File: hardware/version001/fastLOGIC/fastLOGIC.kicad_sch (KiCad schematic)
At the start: 82 parts, among them J1 AVR-ISP-6, J10 0-5V_ANALOG_IN_A, J11 PRES_SENS_BOTTOM, J12 PRES_SENS_TOP, J13 0-5V_ANALOG_IN_B, J14 RELAY_OUT_B, J15 RELAY_OUT_A, J2 USB_B_Micro, J3 DS18B20, J4 12-24V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

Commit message: hardware chnages minor
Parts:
- removed J2: USB_B_Micro, Connector_USB:USB_Micro-B_Amphenol_10118194_Horizontal, symbol Connector:USB_B_Micro
- added J6: USB_B_Mini, Connector_USB:USB_Mini-B_Tensility_54-00023_Vertical, symbol Connector:USB_B_Mini
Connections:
- net GND: now also J6.5 (GND)
- net at C14.2, C15.2, U5.7 (VREGIN)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: now also J6.1 (VBUS)
- net at U5.5 (D-): now also J6.2 (D-)
- net at U5.4 (D+): now also J6.3 (D+)
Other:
- moved on the sheet: C1, C10, C11, C12, C13, C14, C15, C16, C17, C2, C3, C4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

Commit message: latest pcb
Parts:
- U3, U4: footprint Package_DIP:DIP-4_W7.62mm_SMDSocket_SmallPads -> Package_DIP:DIP-4_W8.89mm_SMDSocket_LongPads
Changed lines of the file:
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@@
       (effects (font (size 1.27 1.27)))
     )
-    (property "Footprint" "Package_DIP:DIP-4_W7.62mm_SMDSocket_SmallPads" (at 54.737 194.691 0)
+    (property "Footprint" "Package_DIP:DIP-4_W8.89mm_SMDSocket_LongPads" (at 54.737 194.691 0)
       (effects (font (size 1.27 1.27) italic) (justify left) hide)
     )
@@
       (effects (font (size 1.27 1.27)))
     )
-    (property "Footprint" "Package_DIP:DIP-4_W7.62mm_SMDSocket_SmallPads" (at 91.821 197.993 0)
+    (property "Footprint" "Package_DIP:DIP-4_W8.89mm_SMDSocket_LongPads" (at 91.821 197.993 0)
       (effects (font (size 1.27 1.27) italic) (justify left) hide)
     )

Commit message: minor pcb changes, image
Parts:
- J10, J13, J3: LCSC (none) -> C157928
- J14, J15, J8, J9: LCSC (none) -> C2997510
- J4: LCSC (none) -> C2997509
- J5: LCSC (none) -> C157925
- J6: LCSC (none) -> C6331167
- U7: LCSC (none) -> C38183
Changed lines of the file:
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@@
       (effects (font (size 1.27 1.27)) hide)
     )
+    (property "LCSC" "C157928" (at 229.743 266.827 90)
+      (effects (font (size 1.27 1.27)) hide)
+    )
     (pin "1")
     (pin "2")
@@
       (effects (font (size 1.27 1.27)) hide)
     )
+    (property "LCSC" "C2997509" (at 240.411 266.827 90)
+      (effects (font (size 1.27 1.27)) hide)
+    )
     (pin "1")
     (pin "2")
@@
       (effects (font (size 1.27 1.27)) hide)
     )
+    (property "LCSC" "C2997510" (at 358.013 38.354 90)
+      (effects (font (size 1.27 1.27)) hide)
+    )
     (pin "1")
     (pin "2")
@@
       (effects (font (size 1.27 1.27)) hide)
     )
+    (property "LCSC" "C157928" (at 187.579 266.827 90)
+      (effects (font (size 1.27 1.27)) hide)
+    )
     (pin "1")
     (pin "2")
@@
     )
   )
-  (symbol (lib_id "power:+5V") (at 165.735 117.602 0) (unit 1)
+  (symbol (lib_id "power:+5V") (at 165.735 117.348 0) (unit 1)
     (in_bom yes) (on_board yes) (dnp no) (fields_autoplaced)
-    (property "Reference" "#PWR053" (at 165.735 121.412 0)
+    (property "Reference" "#PWR053" (at 165.735 121.158 0)
       (effects (font (size 1.27 1.27)) hide)
     )
-    (property "Value" "+5V" (at 165.735 113.538 0)
+    (property "Value" "+5V" (at 165.735 113.284 0)
       (effects (font (size 1.27 1.27)))
     )
-    (property "Footprint" "" (at 165.735 117.602 0)
+    (property "Footprint" "" (at 165.735 117.348 0)
       (effects (font (size 1.27 1.27)) hide)
     )
-    (property "Datasheet" "" (at 165.735 117.602 0)
+    (property "Datasheet" "" (at 165.735 117.348 0)
       (effects (font (size 1.27 1.27)) hide)
     )
@@
       (effects (font (size 1.27 1.27)) hide)
     )
+    (property "LCSC" "C157925" (at 257.429 266.827 90)
+      (effects (font (size 1.27 1.27)) hide)
+    )
     (pin "1")
     (pin "2")
@@
     )
   )
-  (symbol (lib_id "Device:C") (at 165.735 121.412 0) (unit 1)
+  (symbol (lib_id "Device:C") (at 165.735 121.158 0) (unit 1)
     (in_bom yes) (on_board yes) (dnp no) (fields_autoplaced)
-    (property "Reference" "C12" (at 168.783 120.777 0)
+    (property "Reference" "C12" (at 168.783 120.523 0)
       (effects (font (size 1.27 1.27)) (justify left))
     )
-    (property "Value" "C100uF" (at 168.783 123.317 0)
+    (property "Value" "C100uF" (at 168.783 123.063 0)
       (effects (font (size 1.27 1.27)) (justify left))
     )
-    (property "Footprint" "Capacitor_SMD:C_1206_3216Metric" (at 166.7002 125.222 0)
+    (property "Footprint" "Capacitor_SMD:C_1206_3216Metric" (at 166.7002 124.968 0)
       (effects (font (size 1.27 1.27)) hide)
     )
-    (property "Datasheet" "~" (at 165.735 121.412 0)
+    (property "Datasheet" "~" (at 165.735 121.158 0)
       (effects (font (size 1.27 1.27)) hide)
     )
-    (property "LCSC" "C15008" (at 165.735 121.412 0)
+    (property "LCSC" "C15008" (at 165.735 121.158 0)
       (effects (font (size 1.27 1.27)) hide)
     )
@@
       (effects (font (size 1.27 1.27)) hide)
     )
+    (property "LCSC" "C2997510" (at 84.201 214.503 90)
+      (effects (font (size 1.27 1.27)) hide)
+    )
     (pin "1")
     (pin "2")
@@
       (effects (font (size 1.27 1.27)) hide)
     )
+    (property "LCSC" "C2997510" (at 47.117 214.249 90)
+      (effects (font (size 1.27 1.27)) hide)
+    )
     (pin "1")
     (pin "2")
@@
       (effects (font (size 1.27 1.27)) hide)
     )
+    (property "LCSC" "C2997510" (at 358.14 87.884 90)
+      (effects (font (size 1.27 1.27)) hide)
+    )
     (pin "1")
     (pin "2")
@@
       (effects (font (size 1.27 1.27)) hide)
     )
+    (property "LCSC" "C38183" (at 244.983 118.999 0)
+      (effects (font (size 1.27 1.27)) hide)
+    )
     (pin "1")
     (pin "10")
@@
     )
   )
-  (symbol (lib_id "power:GND") (at 165.735 125.222 0) (unit 1)
+  (symbol (lib_id "power:GND") (at 165.735 124.968 0) (unit 1)
     (in_bom yes) (on_board yes) (dnp no) (fields_autoplaced)
-    (property "Reference" "#PWR054" (at 165.735 131.572 0)
+    (property "Reference" "#PWR054" (at 165.735 131.318 0)
       (effects (font (size 1.27 1.27)) hide)
     )
-    (property "Value" "GND" (at 165.735 129.794 0)
+    (property "Value" "GND" (at 165.735 129.54 0)
       (effects (font (size 1.27 1.27)))
     )
-    (property "Footprint" "" (at 165.735 125.222 0)
+    (property "Footprint" "" (at 165.735 124.968 0)
       (effects (font (size 1.27 1.27)) hide)
     )
-    (property "Datasheet" "" (at 165.735 125.222 0)
+    (property "Datasheet" "" (at 165.735 124.968 0)
       (effects (font (size 1.27 1.27)) hide)
     )
@@
       (effects (font (size 1.27 1.27)) hide)
     )
+    (property "LCSC" "C6331167" (at 35.814 64.897 0)
+      (effects (font (size 1.27 1.27)) hide)
+    )
     (pin "1")
     (pin "2")
@@
       (effects (font (size 1.27 1.27)) hide)
     )
+    (property "LCSC" "C157928" (at 207.264 266.827 90)
+      (effects (font (size 1.27 1.27)) hide)
+    )

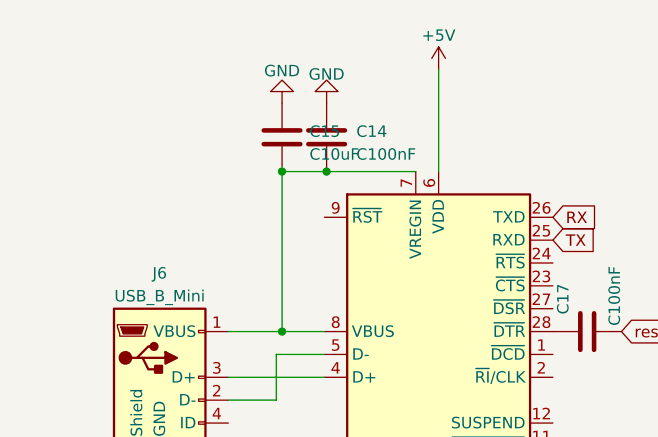
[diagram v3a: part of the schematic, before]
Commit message: Added Pull Up Resistor on CP2102 RST Pin
As per the datasheet Typical Connection Diagrams, a 1kΩ pull-up on the RST is recommended
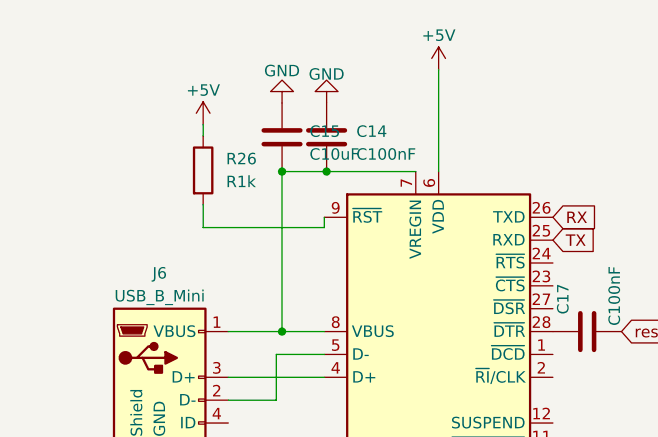
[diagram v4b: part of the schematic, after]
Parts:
- added R26: R1k, Resistor_SMD:R_0603_1608Metric, symbol Device:R
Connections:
- net +5V: now also R26.1
- net at U5.9 (~{RST}): now also R26.2
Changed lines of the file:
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@@
+    (stroke (width 0) (type default))
+  )
+  (wire (pts (xy 40.64 48.26) (xy 40.64 45.72))
     (stroke (width 0) (type default))
   )
@@
     (stroke (width 0) (type default))
   )
+  (wire (pts (xy 54.102 48.26) (xy 54.102 47.117))
+    (stroke (width 0) (type default))
+  )
+  (wire (pts (xy 40.64 36.83) (xy 40.64 38.1))
+    (stroke (width 0) (type default))
+  )
   (wire (pts (xy 272.923 129.159) (xy 275.463 129.159))
     (stroke (width 0) (type default))
@@
   )
   (wire (pts (xy 66.802 30.734) (xy 66.802 42.037))
+    (stroke (width 0) (type default))
+  )
+  (wire (pts (xy 40.64 48.26) (xy 54.102 48.26))
     (stroke (width 0) (type default))
   )
@@
         (path "/467e73ff-605e-4cd5-9b39-76afb3f5d14a"
           (reference "J3") (unit 1)
+        )
+      )
+    )
+  )
+  (symbol (lib_id "power:+5V") (at 40.64 36.83 0) (unit 1)
+    (in_bom yes) (on_board yes) (dnp no) (fields_autoplaced)
+    (property "Reference" "#PWR016" (at 40.64 40.64 0)
+      (effects (font (size 1.27 1.27)) hide)
+    )
+    (property "Value" "+5V" (at 40.64 33.02 0)
+      (effects (font (size 1.27 1.27)))
+    )
+    (property "Footprint" "" (at 40.64 36.83 0)
+      (effects (font (size 1.27 1.27)) hide)
+    )
+    (property "Datasheet" "" (at 40.64 36.83 0)
+      (effects (font (size 1.27 1.27)) hide)
+    )
+    (pin "1")
+    (instances
+      (project "fastLOGIC"
+        (path "/467e73ff-605e-4cd5-9b39-76afb3f5d14a"
+          (reference "#PWR016") (unit 1)
         )
       )
@@
         )
       )
+    )
+  )
+  (symbol (lib_id "Device:R") (at 40.64 41.91 0) (unit 1)
+    (in_bom yes) (on_board yes) (dnp no) (fields_autoplaced)
+    (property "Reference" "R26" (at 43.18 40.64 0)
+      (effects (font (size 1.27 1.27)) (justify left))
+    )
+    (property "Value" "R1k" (at 43.18 43.18 0)
+      (effects (font (size 1.27 1.27)) (justify left))
+    )
+    (property "Footprint" "Resistor_SMD:R_0603_1608Metric" (at 38.862 41.91 90)
+      (effects (font (size 1.27 1.27)) hide)
+    )
+    (property "Datasheet" "~" (at 40.64 41.91 0)
+      (effects (font (size 1.27 1.27)) hide)
+    )
+    (property "LCSC" "C25804" (at 40.64 41.91 0)
+      (effects (font (size 1.27 1.27)) hide)
+    )
+    (pin "1")
+    (pin "2")
+    (instances
+      (project "fastLOGIC"
+        (path "/467e73ff-605e-4cd5-9b39-76afb3f5d14a"
+          (reference "R26") (unit 1)
+        )
+      )
